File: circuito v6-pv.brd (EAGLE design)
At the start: 90.5 x 59.5 mm, 62 parts, among them IC1 LM324N

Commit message: Cambio de resistencias de 100k a 10k
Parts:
- R11, R12, R13, R14, R16, R17, R19, R20, R5, R6, R8, R9: value 100k -> 10k
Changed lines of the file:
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@@
 <attribute name="VALUE" x="19.905" y="51.695" size="1.27" layer="27" rot="R270"/>
 </element>
-<element name="R5" library="rcl" library_urn="urn:adsk.eagle:library:334" package="0207/7" package3d_urn="urn:adsk.eagle:package:23493/1" value="100k" x="45" y="14.75" smashed="yes" rot="R90">
+<element name="R5" library="rcl" library_urn="urn:adsk.eagle:library:334" package="0207/7" package3d_urn="urn:adsk.eagle:package:23493/1" value="10k" x="45" y="14.75" smashed="yes" rot="R90">
 <attribute name="NAME" x="43.603" y="12.21" size="1.27" layer="25" ratio="10" rot="R90"/>
 <attribute name="SPICEPREFIX" value="R" x="45" y="14.75" size="1.778" layer="27" rot="R90" display="off"/>
 <attribute name="VALUE" x="45.5588" y="12.464" size="1.27" layer="27" ratio="10" rot="R90"/>
 </element>
-<element name="R6" library="rcl" library_urn="urn:adsk.eagle:library:334" package="0207/7" package3d_urn="urn:adsk.eagle:package:23493/1" value="100k" x="58" y="14.75" smashed="yes" rot="R270">
+<element name="R6" library="rcl" library_urn="urn:adsk.eagle:library:334" package="0207/7" package3d_urn="urn:adsk.eagle:package:23493/1" value="10k" x="58" y="14.75" smashed="yes" rot="R270">
 <attribute name="NAME" x="59.397" y="17.29" size="1.27" layer="25" ratio="10" rot="R270"/>
 <attribute name="SPICEPREFIX" value="R" x="58" y="14.75" size="1.778" layer="27" rot="R270" display="off"/>
@@
 <attribute name="VALUE" x="49.53" y="47.745" size="1.27" layer="27"/>
 </element>
-<element name="R8" library="rcl" library_urn="urn:adsk.eagle:library:334" package="0207/7" package3d_urn="urn:adsk.eagle:package:23493/1" value="100k" x="32.5" y="20.25" smashed="yes" rot="R180">
+<element name="R8" library="rcl" library_urn="urn:adsk.eagle:library:334" package="0207/7" package3d_urn="urn:adsk.eagle:package:23493/1" value="10k" x="32.5" y="20.25" smashed="yes" rot="R180">
 <attribute name="NAME" x="35.04" y="18.853" size="1.27" layer="25" ratio="10" rot="R180"/>
 <attribute name="SPICEPREFIX" value="R" x="32.5" y="20.25" size="1.778" layer="27" rot="R180" display="off"/>
 <attribute name="VALUE" x="34.786" y="20.8088" size="1.27" layer="27" ratio="10" rot="R180"/>
 </element>
-<element name="R9" library="rcl" library_urn="urn:adsk.eagle:library:334" package="0207/7" package3d_urn="urn:adsk.eagle:package:23493/1" value="100k" x="27.75" y="43" smashed="yes" rot="R270">
+<element name="R9" library="rcl" library_urn="urn:adsk.eagle:library:334" package="0207/7" package3d_urn="urn:adsk.eagle:package:23493/1" value="10k" x="27.75" y="43" smashed="yes" rot="R270">
 <attribute name="NAME" x="29.147" y="45.54" size="1.27" layer="25" ratio="10" rot="R270"/>
 <attribute name="SPICEPREFIX" value="R" x="27.75" y="43" size="1.778" layer="27" rot="R270" display="off"/>
@@
 <attribute name="VALUE" x="29.98" y="47.575" size="1.27" layer="27"/>
 </element>
-<element name="R11" library="rcl" library_urn="urn:adsk.eagle:library:334" package="0207/7" package3d_urn="urn:adsk.eagle:package:23493/1" value="100k" x="46.25" y="40.25" smashed="yes" rot="R180">
+<element name="R11" library="rcl" library_urn="urn:adsk.eagle:library:334" package="0207/7" package3d_urn="urn:adsk.eagle:package:23493/1" value="10k" x="46.25" y="40.25" smashed="yes" rot="R180">
 <attribute name="NAME" x="48.79" y="38.853" size="1.27" layer="25" ratio="10" rot="R180"/>
 <attribute name="SPICEPREFIX" value="R" x="46.25" y="40.25" size="1.778" layer="27" rot="R180" display="off"/>
 <attribute name="VALUE" x="48.536" y="40.8088" size="1.27" layer="27" ratio="10" rot="R180"/>
 </element>
-<element name="R12" library="rcl" library_urn="urn:adsk.eagle:library:334" package="0207/7" package3d_urn="urn:adsk.eagle:package:23493/1" value="100k" x="42.25" y="46.25" smashed="yes" rot="R270">
+<element name="R12" library="rcl" library_urn="urn:adsk.eagle:library:334" package="0207/7" package3d_urn="urn:adsk.eagle:package:23493/1" value="10k" x="42.25" y="46.25" smashed="yes" rot="R270">
 <attribute name="NAME" x="43.647" y="48.79" size="1.27" layer="25" ratio="10" rot="R270"/>
 <attribute name="SPICEPREFIX" value="R" x="42.25" y="46.25" size="1.778" layer="27" rot="R270" display="off"/>
@@
 <attribute name="VALUE" x="35.36" y="47.575" size="1.27" layer="27"/>
 </element>
-<element name="R13" library="rcl" library_urn="urn:adsk.eagle:library:334" package="0207/7" package3d_urn="urn:adsk.eagle:package:23493/1" value="100k" x="60.25" y="38" smashed="yes" rot="R180">
+<element name="R13" library="rcl" library_urn="urn:adsk.eagle:library:334" package="0207/7" package3d_urn="urn:adsk.eagle:package:23493/1" value="10k" x="60.25" y="38" smashed="yes" rot="R180">
 <attribute name="NAME" x="62.79" y="36.603" size="1.27" layer="25" ratio="10" rot="R180"/>
 <attribute name="SPICEPREFIX" value="R" x="60.25" y="38" size="1.778" layer="27" rot="R180" display="off"/>
 <attribute name="VALUE" x="62.536" y="38.5588" size="1.27" layer="27" ratio="10" rot="R180"/>
 </element>
-<element name="R14" library="rcl" library_urn="urn:adsk.eagle:library:334" package="0207/7" package3d_urn="urn:adsk.eagle:package:23493/1" value="100k" x="32.25" y="32" smashed="yes">
+<element name="R14" library="rcl" library_urn="urn:adsk.eagle:library:334" package="0207/7" package3d_urn="urn:adsk.eagle:package:23493/1" value="10k" x="32.25" y="32" smashed="yes">
 <attribute name="NAME" x="29.71" y="33.397" size="1.27" layer="25" ratio="10"/>
 <attribute name="SPICEPREFIX" value="R" x="32.25" y="32" size="1.778" layer="27" display="off"/>
@@
 <attribute name="VALUE" x="57.15" y="47.745" size="1.27" layer="27"/>
 </element>
-<element name="R16" library="rcl" library_urn="urn:adsk.eagle:library:334" package="0207/7" package3d_urn="urn:adsk.eagle:package:23493/1" value="100k" x="32.5" y="14.25" smashed="yes">
+<element name="R16" library="rcl" library_urn="urn:adsk.eagle:library:334" package="0207/7" package3d_urn="urn:adsk.eagle:package:23493/1" value="10k" x="32.5" y="14.25" smashed="yes">
 <attribute name="NAME" x="29.96" y="15.647" size="1.27" layer="25" ratio="10"/>
 <attribute name="SPICEPREFIX" value="R" x="32.5" y="14.25" size="1.778" layer="27" display="off"/>
 <attribute name="VALUE" x="30.214" y="13.6912" size="1.27" layer="27" ratio="10"/>
 </element>
-<element name="R17" library="rcl" library_urn="urn:adsk.eagle:library:334" package="0207/7" package3d_urn="urn:adsk.eagle:package:23493/1" value="100k" x="34" y="39.25" smashed="yes" rot="R180">
+<element name="R17" library="rcl" library_urn="urn:adsk.eagle:library:334" package="0207/7" package3d_urn="urn:adsk.eagle:package:23493/1" value="10k" x="34" y="39.25" smashed="yes" rot="R180">
 <attribute name="NAME" x="36.54" y="37.853" size="1.27" layer="25" ratio="10" rot="R180"/>
 <attribute name="SPICEPREFIX" value="R" x="34" y="39.25" size="1.778" layer="27" rot="R180" display="off"/>
@@
 <attribute name="VALUE" x="32.65" y="47.575" size="1.27" layer="27"/>
 </element>
-<element name="R19" library="rcl" library_urn="urn:adsk.eagle:library:334" package="0207/7" package3d_urn="urn:adsk.eagle:package:23493/1" value="100k" x="46.25" y="35.5" smashed="yes" rot="R180">
+<element name="R19" library="rcl" library_urn="urn:adsk.eagle:library:334" package="0207/7" package3d_urn="urn:adsk.eagle:package:23493/1" value="10k" x="46.25" y="35.5" smashed="yes" rot="R180">
 <attribute name="NAME" x="48.79" y="34.103" size="1.27" layer="25" ratio="10" rot="R180"/>
 <attribute name="SPICEPREFIX" value="R" x="46.25" y="35.5" size="1.778" layer="27" rot="R180" display="off"/>
 <attribute name="VALUE" x="48.536" y="36.0588" size="1.27" layer="27" ratio="10" rot="R180"/>
 </element>
-<element name="R20" library="rcl" library_urn="urn:adsk.eagle:library:334" package="0207/7" package3d_urn="urn:adsk.eagle:package:23493/1" value="100k" x="33.75" y="46.75" smashed="yes" rot="R180">
+<element name="R20" library="rcl" library_urn="urn:adsk.eagle:library:334" package="0207/7" package3d_urn="urn:adsk.eagle:package:23493/1" value="10k" x="33.75" y="46.75" smashed="yes" rot="R180">
 <attribute name="NAME" x="36.29" y="45.353" size="1.27" layer="25" ratio="10" rot="R180"/>
 <attribute name="SPICEPREFIX" value="R" x="33.75" y="46.75" size="1.778" layer="27" rot="R180" display="off"/>

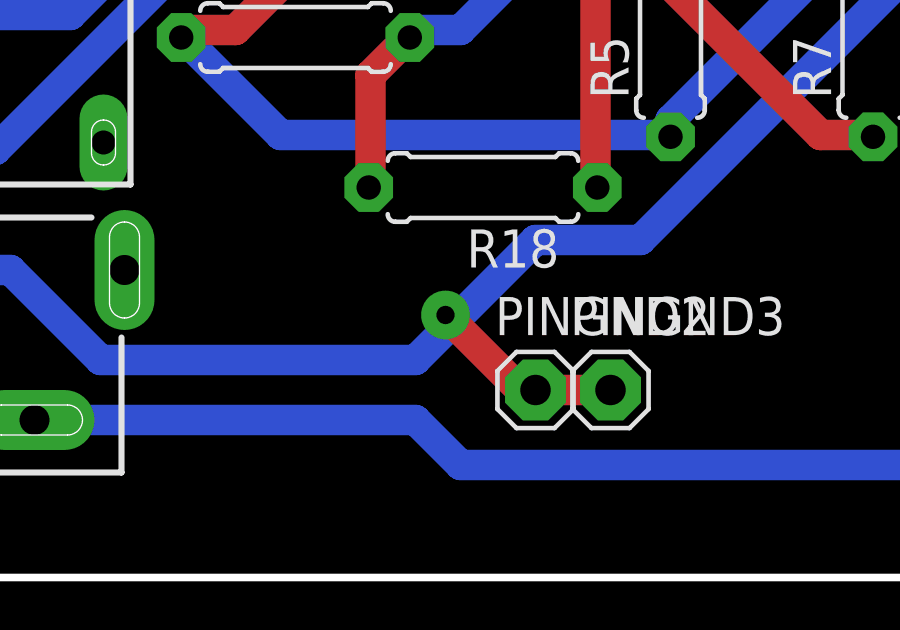
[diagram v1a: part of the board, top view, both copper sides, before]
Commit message: Correccion de via problematica
1. Se corrio levemente de lugar una de las vias problematicas.
2. Se le cambio el tamanio y forma
3. Se activo el menu DRC > Supply > Generate thermals for vias, lo cual le puso esa aislacion a las vias, que era el principal problema.
4. Nuevas versiones del print de los planos
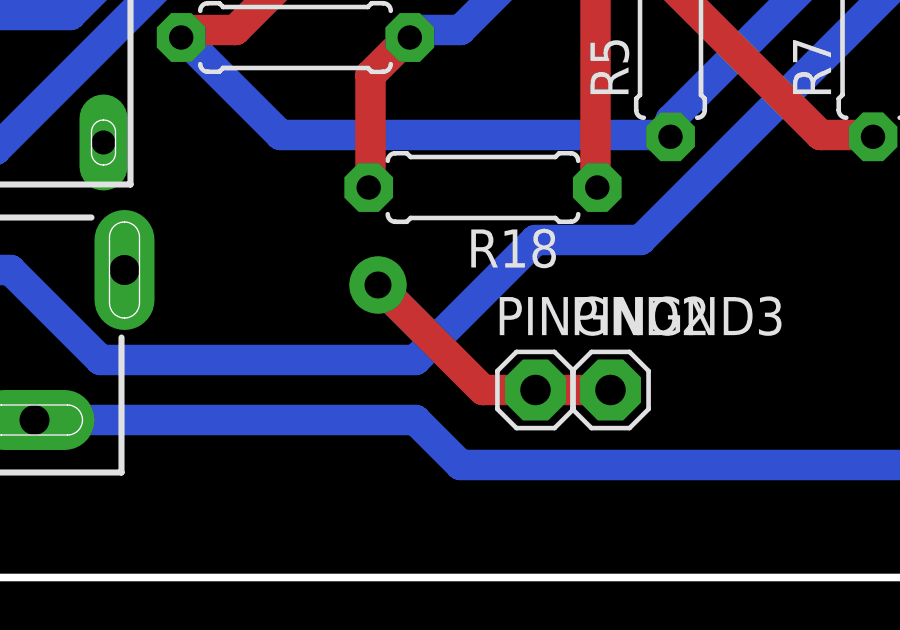
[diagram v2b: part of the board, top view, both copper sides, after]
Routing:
- net GND: track 188.1 -> 193.0 mm

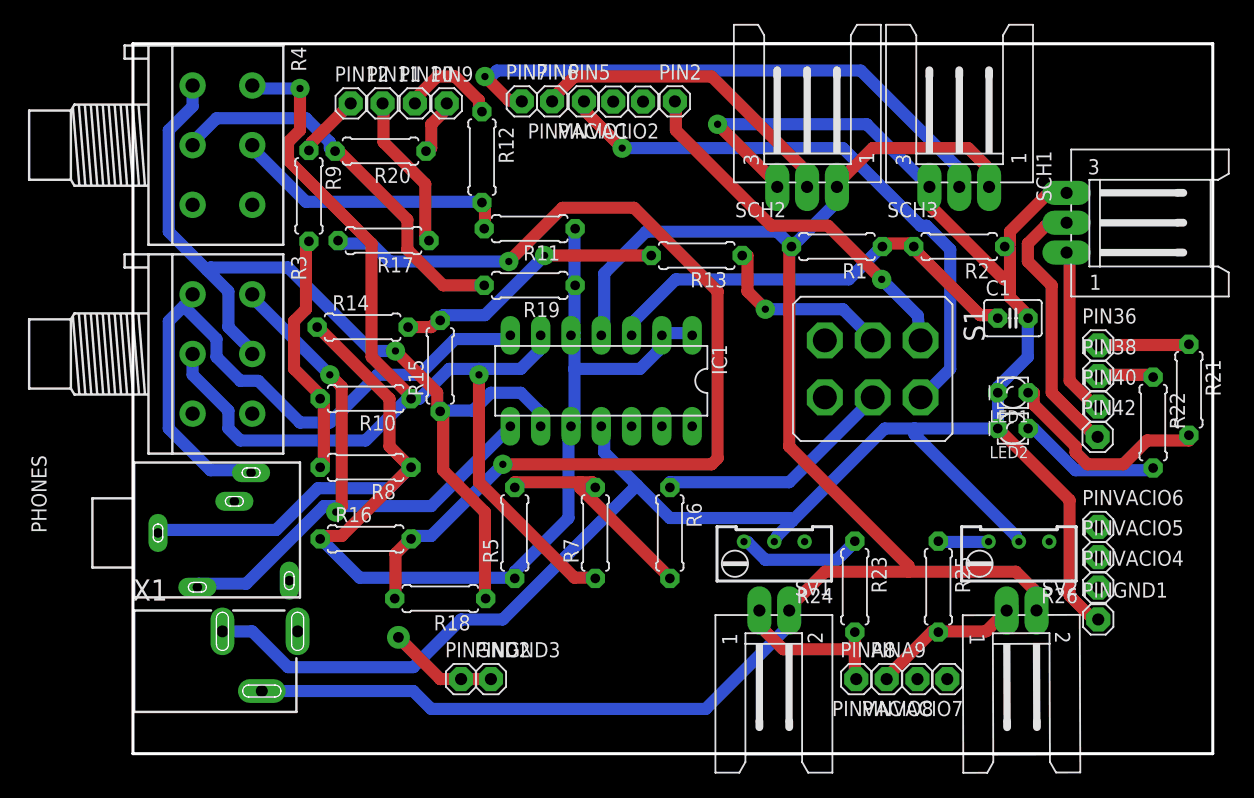
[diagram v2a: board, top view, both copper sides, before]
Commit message: ACTUALIZACION CIRCUITO
Cambios

1- Chequeo de pines/canales/izq y der: 

IZQ - B - 12,9 Y 2
DER - A - 11,10Y5

2- CONEXION TIERRA VIRTUAL A PIN A11

3- CAMBIO DE RESISTENCIAS PARA EL PIN DEL RUIDO

EL POTE PASA A SER DOS Rs DE 100K FIJAS
R11 Y R19 TENIAN 10K Y AHORA TIENEN 1K
R12 Y R20 TENIAN 10K Y AHORA TIENEN 20K

4- SE AGREGAN RESISTENCIAS EN LAS PATAS + DE LOS OPAMPS DE AUDIO (IZQ Y DER)

UNA A TIERRA VIRTUAL DE 10K
OTRA A TIERRA NORMAL DE 100K
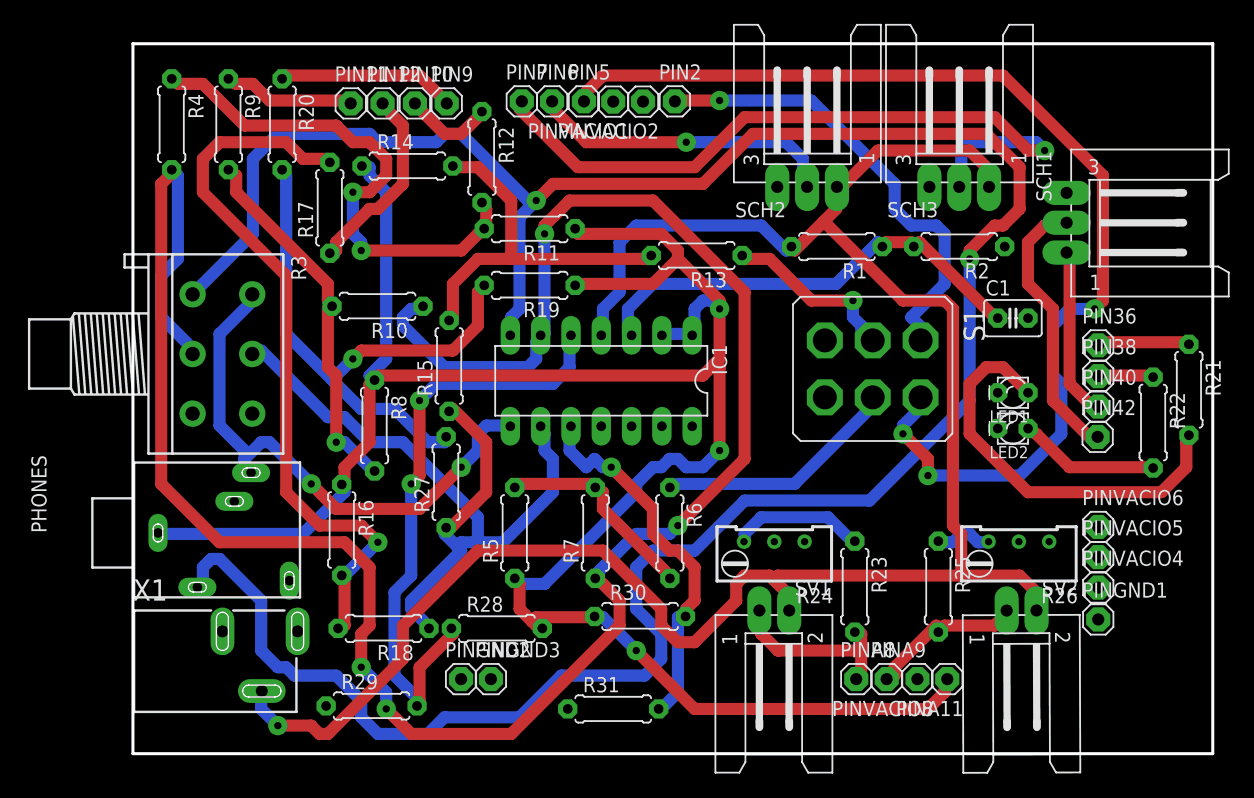
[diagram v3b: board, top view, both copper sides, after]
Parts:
- added R27, R29, R31: 100k, rcl:0207/7
- added R28, R30: 10k, rcl:0207/7
- R11, R19: value 10k -> 1k
- R12, R20: value 10k -> 20k
- R4: device pot:3RP/1610G -> rcl:0207/7
- moved R14 14.0 mm to (36.0, 45.5)
- moved R9 9.03 mm to (21.0, 49.0)
- moved R20 8.55 mm to (25.5, 49.0), turned to 270 degrees
- moved R10 7.81 mm to (33.5, 33.8)
- moved R18 5.37 mm to (34.0, 6.75)
- moved R17 5.27 mm to (29.5, 42.0), turned to 90 degrees
- moved R8 3.58 mm to (33.2, 23.8), turned to 270 degrees
- moved PIN11 2.67 mm to (31.2, 50.8)
- moved PIN12 2.67 mm to (33.9, 50.8)
- moved R4 2.47 mm to (16.2, 49.0)
- moved R16 2.14 mm to (30.5, 15.0), turned to 270 degrees
- moved R15 0.75 mm to (39.5, 28.8)
- renumbered PINVACIO7 to PINA11
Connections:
- new net N$10: IC1.10, R30.2, R31.2
- new net N$17: IC1.5, R28.1, R29.2
- net GND: now also R29.1, R31.1
- net N$11: now also R4.1; no longer R4.2-2
- net N$13: now also R27.1; no longer R4.1-1
- net N$18: now also R27.2; no longer R4.1-2
- net N$20: now also PIN12.1; no longer PIN11.1
- net N$3: now also PIN11.1; no longer PIN12.1
- net N$30: now also PHONES.3; no longer PHONES.2
- net N$37: now also PHONES.2; no longer PHONES.3
- net N$4: now also R4.2; no longer R4.2-1
- net N$8: now also PINA11.1, R28.2, R30.1; no longer IC1.10, IC1.5
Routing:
- net GND: track 193.0 -> 0.00 mm, vias 2 -> 0
- net N$37: track 55.9 -> 213.7 mm, vias 0 -> 2
- net N$4: track 96.1 -> 185.4 mm, vias 2 -> 4
- net N$8: track 109.7 -> 189.8 mm, vias 0 -> 3
- net N$17: track 0.00 -> 51.5 mm, vias 0 -> 2
- net N$7: track 49.7 -> 94.5 mm, vias 1 -> 3
- net N$10: track 0.00 -> 31.9 mm, vias 0 -> 1
- net N$19: track 85.4 -> 61.4 mm, vias 2 -> 1
- net VCC: track 150.9 -> 172.2 mm, vias 0 -> 1
- net N$11: track 23.6 -> 44.1 mm, vias 0 -> 2
- net N$24: track 18.1 -> 34.3 mm
- net N$18: track 33.3 -> 49.1 mm, vias 0 -> 1
- net N$13: track 79.8 -> 67.3 mm, vias 1 -> 0
- net N$28: track 48.8 -> 60.2 mm
- net N$9: track 20.8 -> 31.1 mm, vias 0 -> 1
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
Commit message: ultimo circuito con routeo 100% y 15 vias
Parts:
- moved R15 12.6 mm to (33.8, 40.0), turned to 0 degrees
- moved R17 9.41 mm to (20.2, 40.2), turned to 0 degrees
- moved R1 8.75 mm to (63.2, 38.5)
- moved R13 8.55 mm to (55.0, 44.8)
- moved R2 6.50 mm to (75.8, 39.0)
- moved R27 6.05 mm to (34.0, 22.0), turned to 0 degrees
- moved R16 4.96 mm to (33.8, 11.2), turned to 180 degrees
- moved R8 4.81 mm to (34.0, 28.5), turned to 180 degrees
- moved C1 2.76 mm to (86.5, 35.5)
- moved R18 1.77 mm to (33.8, 8.50)
- moved R10 1.52 mm to (33.8, 35.2)
- moved R29 0.50 mm to (33.0, 0.75)
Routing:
- net N$37: track 213.7 -> 65.2 mm
- net N$4: track 185.4 -> 86.4 mm, vias 4 -> 0
- net N$7: track 94.5 -> 67.0 mm, vias 3 -> 1
- net N$17: track 51.5 -> 75.9 mm
- net N$18: track 49.1 -> 70.0 mm, vias 1 -> 3
- net N$28: track 60.2 -> 41.7 mm
- net N$14: track 31.8 -> 18.7 mm
- net N$19: track 61.4 -> 49.6 mm, vias 1 -> 0
- net VCC: track 172.2 -> 161.5 mm, vias 1 -> 0
- net N$11: track 44.1 -> 33.8 mm, vias 2 -> 0
- net N$8: track 189.8 -> 180.2 mm, vias 3 -> 0
- net N$24: track 34.3 -> 25.2 mm, vias 0 -> 1
- net N$20: track 16.3 -> 24.8 mm
- net N$16: track 39.4 -> 31.5 mm
- net N$15: track 15.7 -> 23.2 mm, vias 1 -> 0
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
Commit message: Actualizacion de resistencias para ruido
Resistencias 200k, 100k y 10k dejan un volumen de ruido tal que no es muy molesto con el estimulo
pero lo suficientemente molesto porque es lo que da el valor maximo
el chiste seria manejar el ruido desde el soft despues
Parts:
- R11: value 1k -> 10k
- R12: value 20k -> 100k
- R4: value 100k -> 200k
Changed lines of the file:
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@@
 <attribute name="VALUE" x="29.98" y="47.575" size="1.27" layer="27"/>
 </element>
-<element name="R11" library="rcl" library_urn="urn:adsk.eagle:library:334" package="0207/7" package3d_urn="urn:adsk.eagle:package:23493/1" value="1k" x="46.25" y="40.25" smashed="yes" rot="R180">
+<element name="R11" library="rcl" library_urn="urn:adsk.eagle:library:334" package="0207/7" package3d_urn="urn:adsk.eagle:package:23493/1" value="10k" x="46.25" y="40.25" smashed="yes" rot="R180">
 <attribute name="NAME" x="48.79" y="38.853" size="1.27" layer="25" ratio="10" rot="R180"/>
 <attribute name="SPICEPREFIX" value="R" x="46.25" y="40.25" size="1.778" layer="27" rot="R180" display="off"/>
 <attribute name="VALUE" x="48.536" y="40.8088" size="1.27" layer="27" ratio="10" rot="R180"/>
 </element>
-<element name="R12" library="rcl" library_urn="urn:adsk.eagle:library:334" package="0207/7" package3d_urn="urn:adsk.eagle:package:23493/1" value="20k" x="42.25" y="46.25" smashed="yes" rot="R270">
+<element name="R12" library="rcl" library_urn="urn:adsk.eagle:library:334" package="0207/7" package3d_urn="urn:adsk.eagle:package:23493/1" value="100k" x="42.25" y="46.25" smashed="yes" rot="R270">
 <attribute name="NAME" x="43.647" y="48.79" size="1.27" layer="25" ratio="10" rot="R270"/>
 <attribute name="SPICEPREFIX" value="R" x="42.25" y="46.25" size="1.778" layer="27" rot="R270" display="off"/>
@@
 <attribute name="VALUE" x="65.475" y="33.58" size="1.778" layer="27" ratio="10" rot="R270"/>
 </element>
-<element name="R4" library="rcl" library_urn="urn:adsk.eagle:library:334" package="0207/7" package3d_urn="urn:adsk.eagle:package:23493/1" value="100k" x="16.25" y="49" smashed="yes" rot="R270">
+<element name="R4" library="rcl" library_urn="urn:adsk.eagle:library:334" package="0207/7" package3d_urn="urn:adsk.eagle:package:23493/1" value="200k" x="16.25" y="49" smashed="yes" rot="R270">
 <attribute name="NAME" x="17.647" y="51.54" size="1.27" layer="25" ratio="10" rot="R270"/>
 <attribute name="SPICEPREFIX" value="R" x="16.25" y="49" size="1.778" layer="27" rot="R270" display="off"/>

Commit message: Actualizacion R fija para ruido 32k
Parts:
- R4: value 200k -> 320k
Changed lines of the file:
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@@
 <attribute name="VALUE" x="65.475" y="33.58" size="1.778" layer="27" ratio="10" rot="R270"/>
 </element>
-<element name="R4" library="rcl" library_urn="urn:adsk.eagle:library:334" package="0207/7" package3d_urn="urn:adsk.eagle:package:23493/1" value="200k" x="16.25" y="49" smashed="yes" rot="R270">
+<element name="R4" library="rcl" library_urn="urn:adsk.eagle:library:334" package="0207/7" package3d_urn="urn:adsk.eagle:package:23493/1" value="320k" x="16.25" y="49" smashed="yes" rot="R270">
 <attribute name="NAME" x="17.647" y="51.54" size="1.27" layer="25" ratio="10" rot="R270"/>
 <attribute name="SPICEPREFIX" value="R" x="16.25" y="49" size="1.778" layer="27" rot="R270" display="off"/>
